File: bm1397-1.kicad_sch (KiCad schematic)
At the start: 58 parts, among them IC1 BM1397_mode1, J8 Conn_01x05, U5 MCP1824T-1802E, U6 MCP1824T-0802E, X1 OT322525MJBA4SL

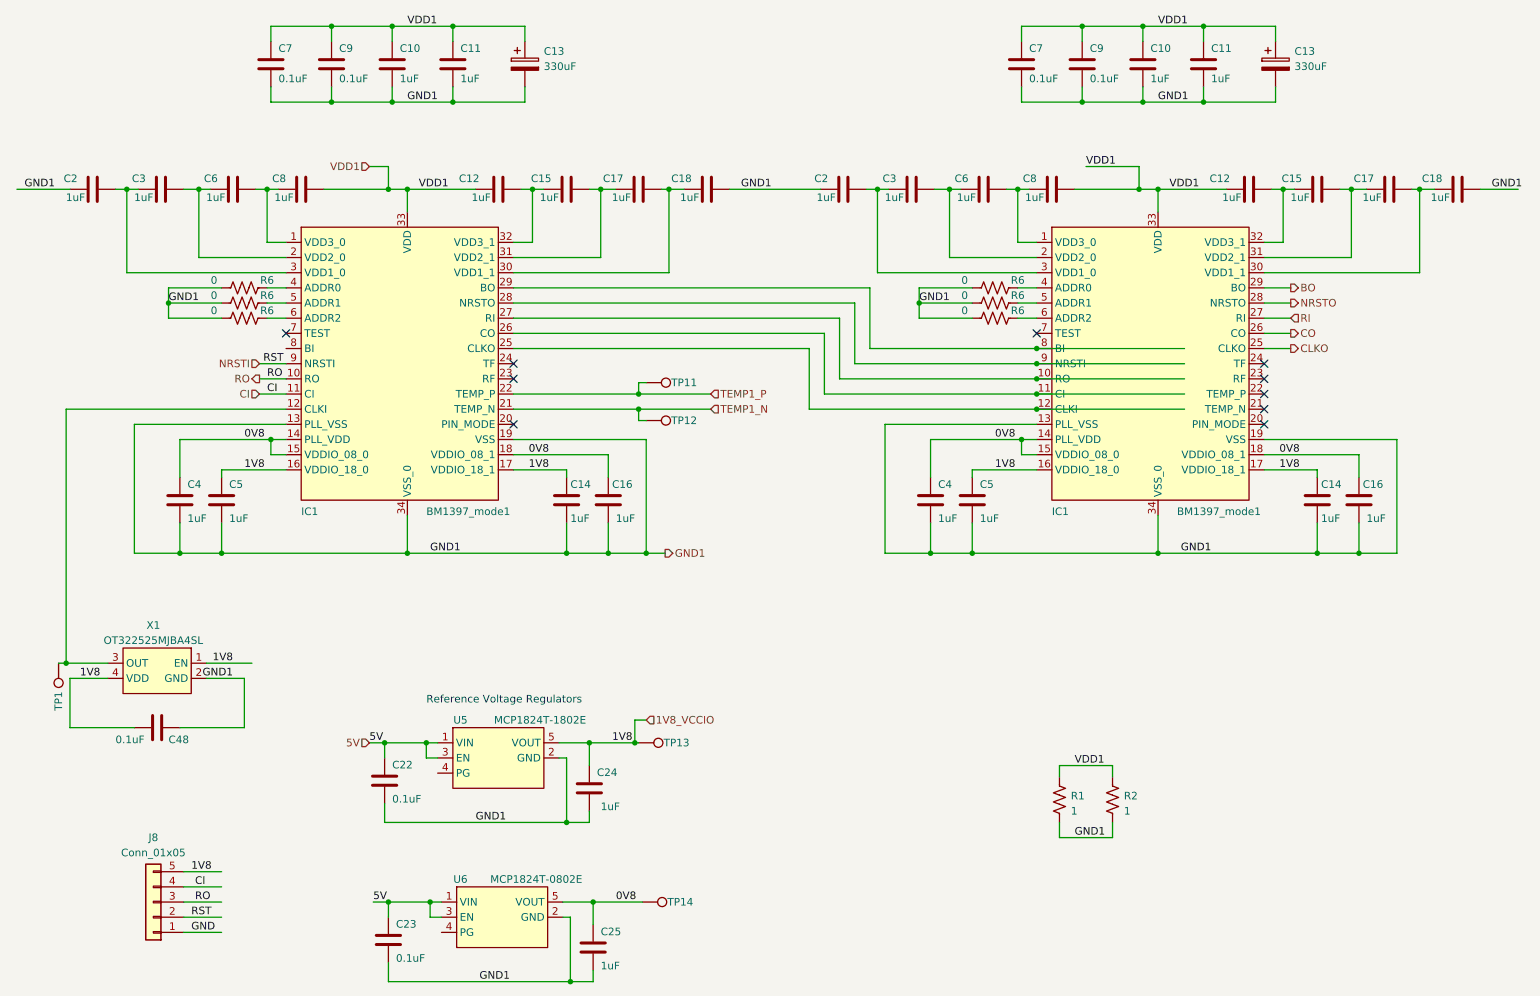
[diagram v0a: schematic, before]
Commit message: update with BM1366
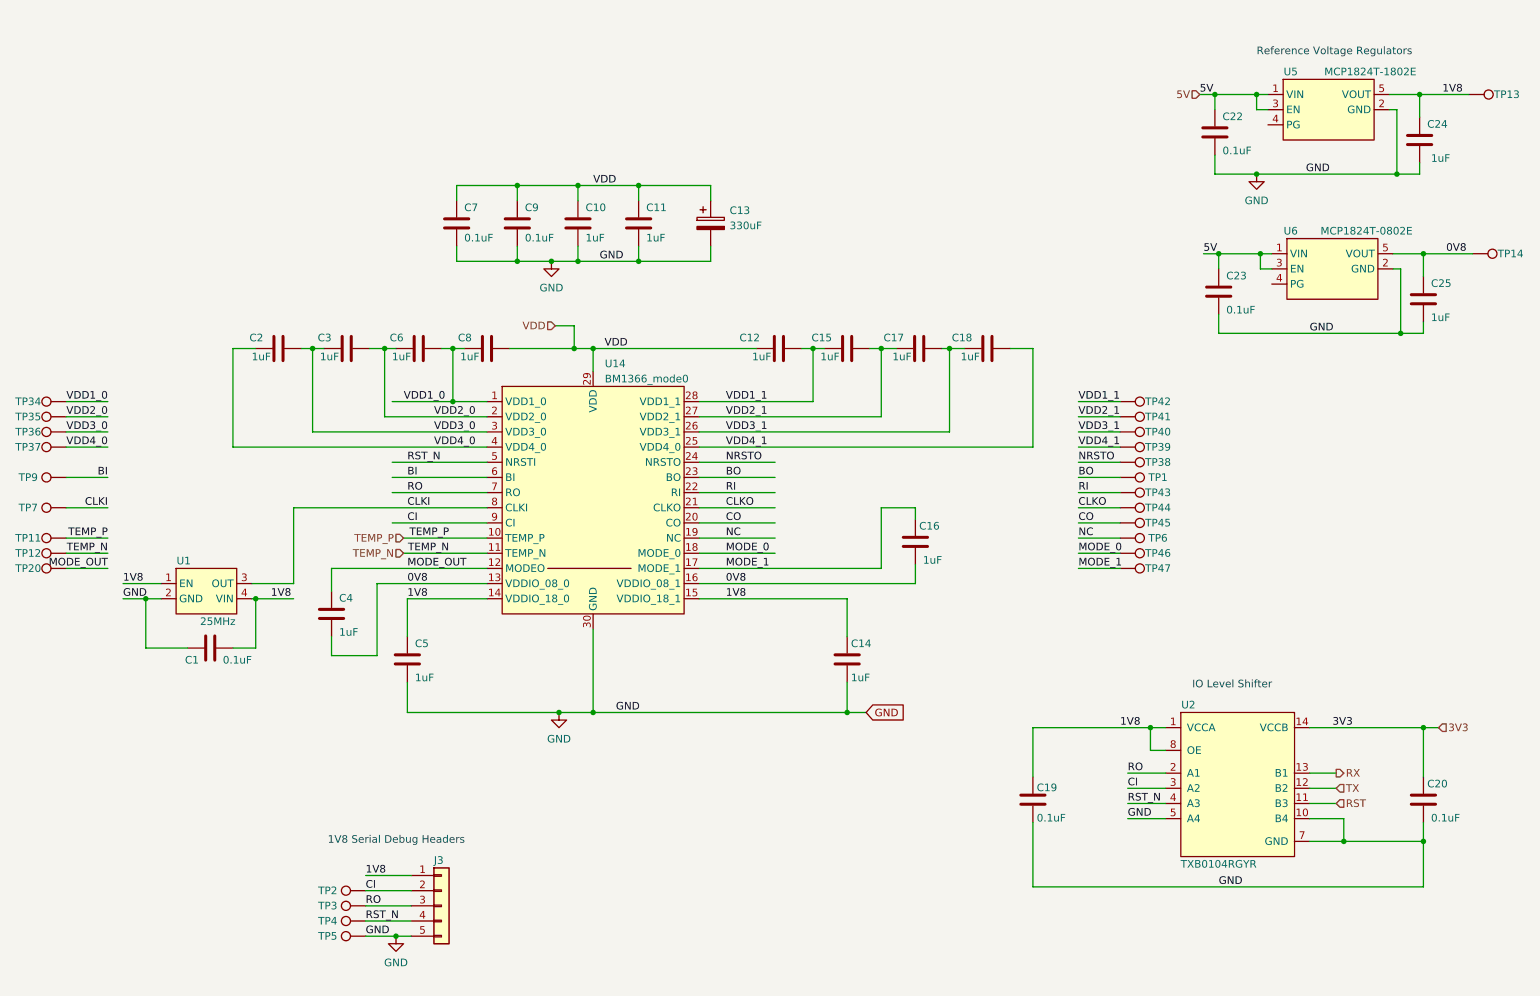
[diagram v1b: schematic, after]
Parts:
- removed C10 (x2), C11 (x2), C12 (x2), C14 (x2), C15 (x2), C16 (x2), C17 (x2), C18 (x2), C2 (x2), C3 (x2), C4 (x2), C5 (x2), C6 (x2), C8 (x2): 587-5514-1-ND, Capacitor_SMD:C_0402_1005Metric, symbol Device:C
- removed C13 (x2): 330uF, Capacitor_Tantalum_SMD:CP_EIA-7343-31_Kemet-D_Pad2.25x2.55mm_HandSolder, symbol Device:C_Polarized
- removed C48, C7 (x2), C9 (x2): 311-3342-1-ND, Capacitor_SMD:C_0402_1005Metric, symbol Device:C
- removed IC1 (x2): BM1397_mode1, bitaxe:BM1397, symbol bitaxe:BM1397_mode1
- removed J8: Conn_01x05, Connector_PinHeader_2.54mm:PinHeader_1x05_P2.54mm_Vertical, symbol Connector_Generic:Conn_01x05
- removed R1, R2: 1, Resistor_SMD:R_2512_6332Metric, symbol Device:R_US
- removed R6 (x6): 0, Resistor_SMD:R_0402_1005Metric, symbol Device:R_US
- removed X1: OT322525MJBA4SL, lcsc:OSC-SMD_4P-L3.2-W2.5-BL, symbol lcsc:OT322525MJBA4SL
- added C1, C19, C20, C7, C9: 0.1uF, Capacitor_SMD:C_0402_1005Metric, symbol Device:C
- added C10, C11, C12, C14, C15, C16, C17, C18, C2, C3, C4, C5, C6, C8: 1uF, Capacitor_SMD:C_0402_1005Metric, symbol Device:C
- added C13: 330uF, Capacitor_Tantalum_SMD:CP_EIA-7343-31_Kemet-D_Pad2.25x2.55mm_HandSolder, symbol Device:C_Polarized
- added J3: Conn_01x05, Connector_PinHeader_2.54mm:PinHeader_1x05_P2.54mm_Vertical, symbol Connector_Generic:Conn_01x05
- added TP2, TP20, TP3, TP34, TP35, TP36, TP37, TP38, TP39, TP4, TP40, TP41, TP42, TP43, TP44, TP45, TP46, TP47, TP5, TP6, TP7, TP9: TestPoint, TestPoint:TestPoint_Pad_D1.5mm, symbol Connector:TestPoint
- added U1: 25MHz, bitaxe:O 25,0-JO32-B-1V3-1-T1-LF, symbol bitaxe:oscillator
- added U14: BM1366_mode0, bitaxe:BM1366, symbol Bitaxe:BM1366_mode1
- added U2: TXB0104RGYR, bitaxe:TXB0104, symbol bitaxe:TXB0104RGYR
- C22, C23: value 311-3342-1-ND -> 0.1uF
- TP1, TP11, TP12: DNP T -> (none); now left out of the parts list
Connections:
- net GND1 is gone; now on net GND: C22.2, C23.2, C24.2, C25.2, U5.2 (GND), U6.2 (GND)
- net 0V8: now also C16.2, C4.2, U14.13 (VDDIO_08_0), U14.16 (VDDIO_08_1)
- net BO: now also TP1.1, U14.23 (BO)
- net CI: now also J3.2 (Pin_2), TP2.1, U14.9 (CI), U2.3 (A2)
- net CLKO: now also TP44.1, U14.21 (CLKO)
- net CO: now also TP45.1, U14.20 (CO)
- net GND: now also C1.1, C10.2, C11.2, C13.2, C14.2, C19.2, C20.2, C5.2, C7.2, C9.2, J3.5 (Pin_5), TP5.1, U1.2 (GND), U14.30 (GND), U2.10 (B4), U2.15 (GND), U2.16 (GND), U2.17 (GND), U2.18 (GND), U2.19 (GND), U2.5 (A4), U2.7 (GND)
- net NRSTO: now also TP38.1, U14.24 (NRSTO)
- net RI: now also TP43.1, U14.22 (RI)
- net RO: now also J3.3 (Pin_3), TP3.1, U14.7 (RO), U2.2 (A1)
- net 1V8_VCCIO renamed 1V8
- net 1V8: now also C1.2, C14.1, C19.1, C5.1, J3.1 (Pin_1), U1.1 (EN), U1.4 (VIN), U14.14 (VDDIO_18_0), U14.15 (VDDIO_18_1), U2.1 (VCCA), U2.8 (OE)
- net TEMP1_N renamed TEMP_N
- net TEMP_N: now also U14.11 (TEMP_N)
- net TEMP1_P renamed TEMP_P
- net TEMP_P: now also U14.10 (TEMP_P)
- new net 3V3: C20.1, U2.14 (VCCB)
- new net BI: TP9.1, U14.6 (BI)
- new net CLKI: TP7.1, U1.3 (OUT), U14.8 (CLKI)
- new net MODE_0: TP46.1, U14.18 (MODE_0)
- new net MODE_1: C16.1, TP47.1, U14.17 (MODE_1)
- new net MODE_OUT: C4.1, TP20.1, U14.12 (MODEO)
- new net NC: TP6.1, U14.19 (NC)
- new net RST: U2.11 (B3)
- new net RST_N: J3.4 (Pin_4), TP4.1, U14.5 (NRSTI), U2.4 (A3)
- new net RX: U2.13 (B1)
- new net TX: U2.12 (B2)
- new net VDD: C10.1, C11.1, C12.1, C13.1, C7.1, C8.2, C9.1, U14.29 (VDD)
- new net VDD1_0: C6.2, C8.1, TP34.1, U14.1 (VDD1_0)
- new net VDD1_1: C12.2, C15.1, TP42.1, U14.28 (VDD1_1)
- new net VDD2_0: C3.2, C6.1, TP35.1, U14.2 (VDD2_0)
- new net VDD2_1: C15.2, C17.1, TP41.1, U14.27 (VDD2_1)
- new net VDD3_0: C2.2, C3.1, TP36.1, U14.3 (VDD3_0)
- new net VDD3_1: C17.2, C18.1, TP40.1, U14.26 (VDD3_1)
- new net VDD4_0: C2.1, TP37.1, U14.4 (VDD4_0)
- new net VDD4_1: C18.2, TP39.1, U14.25 (VDD4_0)
- no-connect marks 10 -> 0
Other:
- note added: "1V8 Serial Debug Headers"
- note added: "IO Level Shifter"
